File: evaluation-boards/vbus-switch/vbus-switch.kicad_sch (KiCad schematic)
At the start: 83 parts, among them J1 BANANA, J10 01x02, J11 Conn_02x06_Top_Bottom, J2 BANANA, J3 BANANA, J4 USB_C, J5 USB_C, J6 USB_A, J7 01x02, J8 01x02, J9 01x02, Q1 PMOS, Q2 PMOS, Q3 PMOS, Q4 PMOS, Q5 2PMOS, Q6 2NMOS, Q7 2NMOS, U1 PAC195X-1-WLCSP, U2 FUSB302BMPX

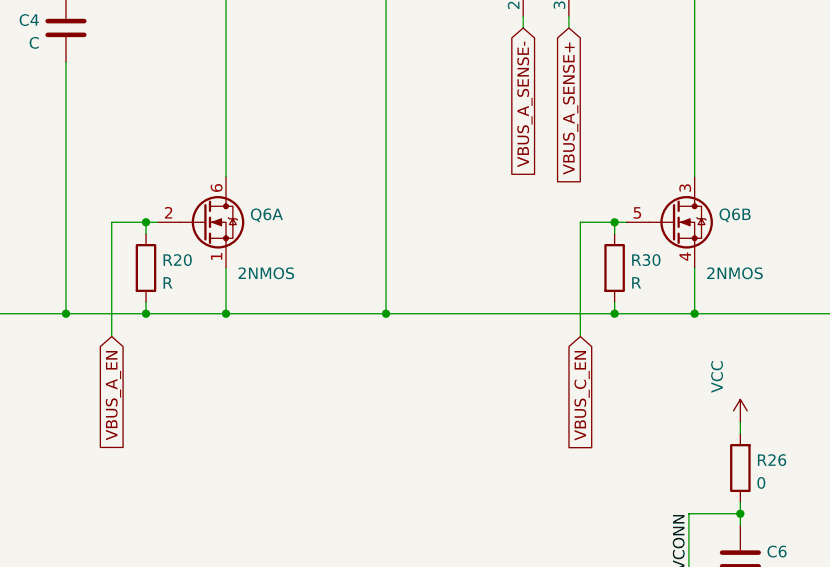
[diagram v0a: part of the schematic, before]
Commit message: vbus-switch: add part selections
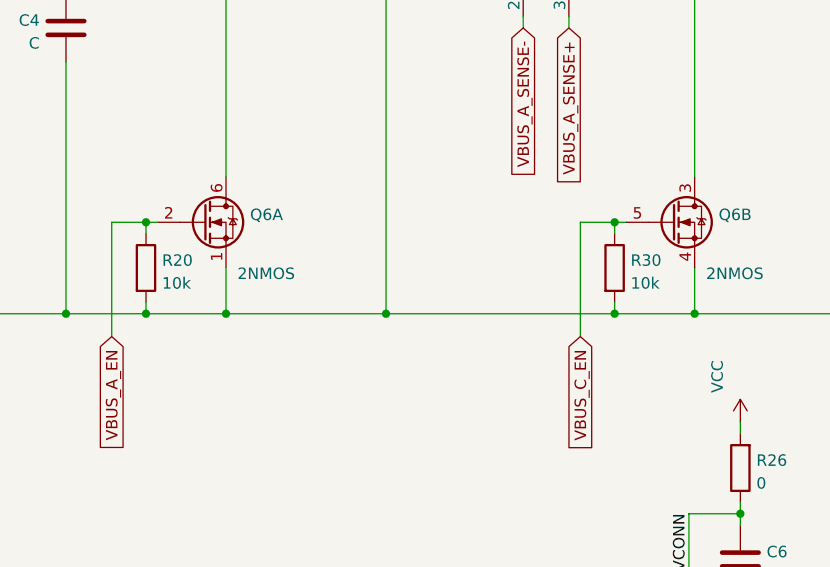
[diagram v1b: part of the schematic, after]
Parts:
- J4, J5: Manufacturer (none) -> XKB; Part Number (none) -> U262-161N-4BVC11
- J6: Manufacturer (none) -> Jing Extension of the Electronic Co.; Part Number (none) -> C42411
- Q1, Q2, Q3, Q4: Manufacturer (none) -> Panjit; Part Number (none) -> PJA3441_R1_00001
- Q5: Manufacturer (none) -> Yangzhou Yangjie; Part Number (none) -> BSS84DW
- Q6, Q7: Manufacturer (none) -> Yangzhou Yangjie; Part Number (none) -> 2N7002DW
- R20, R30: value R -> 10k
- U1: Manufacturer (none) -> Microchip; Part Number (none) -> PAC1954T-E/J6CX
- U2: Manufacturer (none) -> onsemi; Part Number (none) -> FUSB302BMPX
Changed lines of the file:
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@@
+      (effects (font (size 1.27 1.27)) hide)
+    )
+    (property "Manufacturer" "Yangzhou Yangjie" (id 4) (at 191.77 35.56 0)
+      (effects (font (size 1.27 1.27)) hide)
+    )
+    (property "Part Number" "BSS84DW" (id 5) (at 191.77 35.56 0)
       (effects (font (size 1.27 1.27)) hide)
     )
@@
     )
     (property "Datasheet" "~" (id 3) (at 140.97 35.56 0)
+      (effects (font (size 1.27 1.27)) hide)
+    )
+    (property "Manufacturer" "Yangzhou Yangjie" (id 4) (at 139.7 35.56 0)
+      (effects (font (size 1.27 1.27)) hide)
+    )
+    (property "Part Number" "BSS84DW" (id 5) (at 139.7 35.56 0)
       (effects (font (size 1.27 1.27)) hide)
     )
@@
       (effects (font (size 1.27 1.27)) (justify left))
     )
-    (property "Value" "R" (id 1) (at 124.968 85.5222 0)
+    (property "Value" "10k" (id 1) (at 124.968 85.5222 0)
       (effects (font (size 1.27 1.27)) (justify left))
     )
@@
     )
     (property "Datasheet" "" (id 3) (at 103.505 173.355 0)
+      (effects (font (size 1.27 1.27)) hide)
+    )
+    (property "Manufacturer" "Microchip" (id 4) (at 103.505 173.355 0)
+      (effects (font (size 1.27 1.27)) hide)
+    )
+    (property "Part Number" "PAC1954T-E/J6CX" (id 5) (at 103.505 173.355 0)
       (effects (font (size 1.27 1.27)) hide)
     )
@@
       (effects (font (size 1.27 1.27)) hide)
     )
+    (property "Manufacturer" "Panjit" (id 4) (at 93.98 35.56 0)
+      (effects (font (size 1.27 1.27)) hide)
+    )
+    (property "Part Number" "PJA3441_R1_00001" (id 5) (at 93.98 35.56 0)
+      (effects (font (size 1.27 1.27)) hide)
+    )
     (pin "1")
     (pin "2")
@@
     )
     (property "Datasheet" "~" (id 3) (at 72.39 35.56 0)
+      (effects (font (size 1.27 1.27)) hide)
+    )
+    (property "Manufacturer" "Panjit" (id 4) (at 72.39 35.56 0)
+      (effects (font (size 1.27 1.27)) hide)
+    )
+    (property "Part Number" "PJA3441_R1_00001" (id 5) (at 72.39 35.56 0)
       (effects (font (size 1.27 1.27)) hide)
     )
@@
     )
     (property "Datasheet" "https://www.usb.org/sites/default/files/documents/usb_type-c.zip" (id 3) (at 262.255 125.73 0)
+      (effects (font (size 1.27 1.27)) hide)
+    )
+    (property "Manufacturer" "XKB" (id 4) (at 266.065 125.73 0)
+      (effects (font (size 1.27 1.27)) hide)
+    )
+    (property "Part Number" "U262-161N-4BVC11" (id 5) (at 266.065 125.73 0)
       (effects (font (size 1.27 1.27)) hide)
     )
@@
       (effects (font (size 1.27 1.27)) hide)
     )
+    (property "Manufacturer" "Yangzhou Yangjie" (id 4) (at 129.54 78.74 0)
+      (effects (font (size 1.27 1.27)) hide)
+    )
+    (property "Part Number" "2N7002DW" (id 5) (at 129.54 78.74 0)
+      (effects (font (size 1.27 1.27)) hide)
+    )
     (pin "1")
     (pin "2")
@@
       (effects (font (size 1.27 1.27)) hide)
     )
+    (property "Manufacturer" "Panjit" (id 4) (at 210.82 41.91 0)
+      (effects (font (size 1.27 1.27)) hide)
+    )
+    (property "Part Number" "PJA3441_R1_00001" (id 5) (at 210.82 41.91 0)
+      (effects (font (size 1.27 1.27)) hide)
+    )
     (pin "1")
     (pin "2")
@@
       (effects (font (size 1.27 1.27)) (justify left))
     )
-    (property "Value" "R" (id 1) (at 177.038 85.5222 0)
+    (property "Value" "10k" (id 1) (at 177.038 85.5222 0)
       (effects (font (size 1.27 1.27)) (justify left))
     )
@@
       (effects (font (size 1.27 1.27)) hide)
     )
+    (property "Manufacturer" "Jing Extension of the Electronic Co." (id 4) (at 274.955 43.815 0)
+      (effects (font (size 1.27 1.27)) hide)
+    )
+    (property "Part Number" "C42411" (id 5) (at 274.955 43.815 0)
+      (effects (font (size 1.27 1.27)) hide)
+    )
     (pin "1")
     (pin "2")
@@
     )
     (property "Datasheet" "~" (id 3) (at 186.69 78.74 0)
+      (effects (font (size 1.27 1.27)) hide)
+    )
+    (property "Manufacturer" "Yangzhou Yangjie" (id 4) (at 181.61 78.74 0)
+      (effects (font (size 1.27 1.27)) hide)
+    )
+    (property "Part Number" "2N7002DW" (id 5) (at 181.61 78.74 0)
       (effects (font (size 1.27 1.27)) hide)
     )
@@
       (effects (font (size 1.27 1.27)) hide)
     )
+    (property "Manufacturer" "Yangzhou Yangjie" (id 4) (at 82.55 72.39 0)
+      (effects (font (size 1.27 1.27)) hide)
+    )
+    (property "Part Number" "2N7002DW" (id 5) (at 82.55 72.39 0)
+      (effects (font (size 1.27 1.27)) hide)
+    )
     (pin "1")
     (pin "2")
@@
       (effects (font (size 1.27 1.27)) hide)
     )
+    (property "Manufacturer" "Panjit" (id 4) (at 158.75 41.91 0)
+      (effects (font (size 1.27 1.27)) hide)
+    )
+    (property "Part Number" "PJA3441_R1_00001" (id 5) (at 158.75 41.91 0)
+      (effects (font (size 1.27 1.27)) hide)
+    )
     (pin "1")
     (pin "2")
@@
     )
     (property "Datasheet" "http://www.onsemi.com/pub/Collateral/FUSB302B-D.PDF" (id 3) (at 186.055 146.05 0)
+      (effects (font (size 1.27 1.27)) hide)
+    )
+    (property "Manufacturer" "onsemi" (id 4) (at 183.515 135.89 0)
+      (effects (font (size 1.27 1.27)) hide)
+    )
+    (property "Part Number" "FUSB302BMPX" (id 5) (at 183.515 135.89 0)
       (effects (font (size 1.27 1.27)) hide)
     )
@@
     )
     (property "Datasheet" "https://www.usb.org/sites/default/files/documents/usb_type-c.zip" (id 3) (at 33.02 147.32 0)
+      (effects (font (size 1.27 1.27)) hide)
+    )
+    (property "Manufacturer" "XKB" (id 4) (at 29.21 147.32 0)
+      (effects (font (size 1.27 1.27)) hide)
+    )
+    (property "Part Number" "U262-161N-4BVC11" (id 5) (at 29.21 147.32 0)
       (effects (font (size 1.27 1.27)) hide)
     )
@@
       (effects (font (size 1.27 1.27)) hide)
     )
+    (property "Manufacturer" "Yangzhou Yangjie" (id 4) (at 53.975 78.74 0)
+      (effects (font (size 1.27 1.27)) hide)
+    )
+    (property "Part Number" "2N7002DW" (id 5) (at 53.975 78.74 0)
+      (effects (font (size 1.27 1.27)) hide)
+    )
     (pin "1")
     (pin "2")
@@
     )
     (path "/628c65a9-0f43-4685-aa66-ee3ad9642224"
-      (reference "R20") (unit 1) (value "R") (footprint "Resistor_SMD:R_0402_1005Metric")
+      (reference "R20") (unit 1) (value "10k") (footprint "Resistor_SMD:R_0402_1005Metric")
     )
     (path "/1abddf7a-ee92-4556-a8f2-a69dd1f55f62"
@@
     )
     (path "/a4d8816a-0ec1-467c-8ec7-bd93ed44bef5"
-      (reference "R30") (unit 1) (value "R") (footprint "Resistor_SMD:R_0402_1005Metric")
+      (reference "R30") (unit 1) (value "10k") (footprint "Resistor_SMD:R_0402_1005Metric")
     )
     (path "/f2aac2dc-6a47-45ec-8c8f-6020a76a7c4e"

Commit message: update vbus-switch
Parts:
- removed Q5: 2PMOS, Package_TO_SOT_SMD:SOT-363_SC-70-6, symbol Device:Q_Dual_PMOS_S1G1D2S2G2D1
- removed Q6, Q7: 2NMOS, Package_TO_SOT_SMD:SOT-363_SC-70-6, symbol Device:Q_Dual_NMOS_S1G1D2S2G2D1
- removed R31: 20k, Resistor_SMD:R_0402_1005Metric, symbol Device:R
- removed R32, R33: 10k, Resistor_SMD:R_0402_1005Metric, symbol Device:R
- removed R35: 0.02±1%, eval:R_0603_1608Metric_Current_Sense, symbol Device:R_Shunt
- added C11: 2.2uF, Capacitor_SMD:C_0603_1608Metric, symbol Device:C
- added C12: 1uF, Capacitor_SMD:C_0603_1608Metric, symbol Device:C
- added C13, C14, C15, C16: 390pF, Capacitor_SMD:C_0402_1005Metric, symbol Device:C
- added D3, D5: D, Diode_SMD:D_SOD-123F, symbol Device:D_Schottky
- added D4: 6.2±2%, eval:DFN1006-2, symbol Device:D_Zener
- added D6: 18±2%, eval:DFN1006-2, symbol Device:D_Zener
- added D7: 4.7±2%, eval:DFN1006-2, symbol Device:D_Zener
- added J12, J14, J15, J16: 01x02, Connector_PinHeader_2.54mm:PinHeader_1x02_P2.54mm_Vertical, symbol Connector_Generic:Conn_01x02
- added J13: BANANA, Connector:Banana_Jack_2Pin, symbol Connector_Generic:Conn_01x02
- added J17: USB_C, eval:USB_C_Receptacle_HRO_TYPE-C-31-M-12, symbol Connector:USB_C_Receptacle_USB2.0
- added Q1, Q10, Q7: 2NPN, Package_TO_SOT_SMD:SOT-363_SC-70-6, symbol Transistor_BJT:BC847BS
- added Q11, Q12, Q3, Q4: PMOS, Package_TO_SOT_SMD:SOT-23-3, symbol Device:Q_PMOS_GSD
- added Q2: 2PNP, Package_TO_SOT_SMD:SOT-363_SC-70-6, symbol Device:Q_Dual_PNP_PNP_E1B1C2E2B2C1
- added R1, R3, R4, R41, R51: 18.7k±1%, Resistor_SMD:R_0402_1005Metric, symbol Device:R
- added R14, R35, R37, R38, R43, R44, R45: 33k, Resistor_SMD:R_0402_1005Metric, symbol Device:R
- added R40, R42: 2.2k, Resistor_SMD:R_0402_1005Metric, symbol Device:R
- added R46: 0.02±1%, eval:R_0603_1608Metric_Current_Sense, symbol Device:R_Shunt
- added R47: 0, Resistor_SMD:R_0402_1005Metric, symbol Device:R
- added R48: 58.3k±1%, Resistor_SMD:R_0402_1005Metric, symbol Device:R
- added R49, R50, R54: R, Resistor_SMD:R_0402_1005Metric, symbol Device:R
- added R52, R53: 5.1k, Resistor_SMD:R_0402_1005Metric, symbol Device:R
- added TP16: TestPoint, TestPoint:TestPoint_Pad_D1.5mm, symbol Connector:TestPoint
- added U3: AP7361EA-33, Package_DFN_QFN:DFN-8-1EP_3x3mm_P0.65mm_EP1.55x2.4mm, symbol eval:AP7361EA-XXFGE-7
- C1: footprint Capacitor_SMD:C_0805_2012Metric -> Capacitor_SMD:C_0402_1005Metric
- D1: value 5.6±2% -> 4.7±2%; Part Number BZX884-B5V6,315 -> BZX884-B4V7,315
- D2: value 4.7±2% -> 18±2%; DNP (none) -> DNP; Part Number BZX884-B4V7,315 -> BZX884-B18,315
- R13: value 0 -> 2.2k
- R15: value 1k -> 18.7k±1%
- R16: value 20k -> R
- R17, R22, R29, R30: value 10k -> 18.7k±1%
- R18: value 10k -> 33k
- R2, R21: value 20k -> 18.7k±1%
- R20: value 10k -> 2.2k
- R33: renamed from R1; value 20k -> 33k
- R39: renamed from R14; value 1k -> 2.2k
- renumbered Q1 to Q5, Q4 to Q6, Q2 to Q8, Q3 to Q9, R3 to R31, R4 to R32
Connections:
- net VBUS_C_SENSE+ is gone; now on net AUX_SENSE+: U1.A3 (SENSE1+)
- net VBUS_C_SENSE- is gone; now on net AUX_SENSE-: U1.A2 (SENSE1-)
- net +5V: now also C1.1, R16.1, C12.2, D3.1 (K), D4.1 (K), D5.1 (K), J14.1 (Pin_1), J14.2 (Pin_2), U3.5 (EN), U3.8 (IN); no longer C7.1, J1.2 (Pin_2), J4.A4 (VBUS), J4.A9 (VBUS), J4.B4 (VBUS), J4.B9 (VBUS), J7.1 (Pin_1), J7.2 (Pin_2), R32.4
- net GND: now also R16.2, R2.2, R21.2, C11.2, C12.1, C13.1, C14.2, C15.1, C16.2, D4.2 (A), J13.1 (Pin_1), J17.A1 (GND), J17.A12 (GND), J17.B1 (GND), J17.B12 (GND), Q1.1 (E1), Q1.4 (E2), Q10.1 (E1), Q10.4 (E2), Q7.1 (E1), Q7.4 (E2), R37.2, R38.2, R4.2, R43.2, R47.2, R49.2, R50.2, R51.2, R52.2, R53.2, R54.2, U3.4 (GND), U3.9 (GND); no longer D1.2 (A), R20.2, R29.2
- net VCC: now also J16.1 (Pin_1), J16.2 (Pin_2)
- net TARGET_A_VBUS: now reaches Q8.3 (D), R34.1
- net TARGET_A_VBUS: now also Q9.3 (D), TP12.1, Q11.3 (D)
- net AUX_VBUS: now reaches R32.1
- net AUX_VBUS: now also Q6.3 (D), R18.1, R29.1, D6.1 (K), Q2.4 (E2), Q4.3 (D); no longer Q9.3 (D)
- net at R22.1, TP4.1: now also R29.2, D7.1 (K), Q2.5 (B2); no longer R21.1
- net at TP11.1: now also Q6.1 (G), Q9.1 (G), Q7.3 (C2), R35.2
- net at Q8.1 (G), R33.2, TP10.1: now also Q5.1 (G), Q7.6 (C1); no longer R29.1
- net at J4.B5 (CC2), R6.1: now also C15.2
- net at R22.2: now also Q1.3 (C2)
- net CONTROL_VBUS: now reaches R31.4
- net CONTROL_VBUS: now also D2.1 (K), Q5.3 (D), Q2.1 (E1), Q3.3 (D), R1.1, R14.1; no longer Q6.3 (D)
- net at D2.2 (A), R15.1: now also TP2.1, Q2.6 (C1), Q3.1 (G), R14.2; no longer TP13.1
- net at J4.A5 (CC1), R7.1: now also C16.1
- net at R18.2: now also R17.1, TP3.1, D6.2 (A), Q2.3 (C2), Q4.1 (G)
- net 5V_OUT_EN renamed CONTROL_VBUS_EN
- net 5V_SENSE+ renamed AUX_SENSE+
- net AUX_SENSE+: no longer U1.D3 (SENSE4+)
- net 5V_SENSE- renamed AUX_SENSE-
- net AUX_SENSE-: no longer U1.D2 (SENSE4-)
- net CAP_SENSE+ renamed CONTROL_SENSE+
- net CONTROL_SENSE+: now also U1.A1 (SENSE2+); no longer U1.D1 (SENSE3+)
- net CAP_SENSE- renamed CONTROL_SENSE-
- net CONTROL_SENSE-: now also U1.B1 (SENSE2-); no longer U1.C1 (SENSE3-)
- removed net VBUS: C4.1, D2.1 (K), Q5.2 (S), Q6.2 (S), Q8.2 (S), Q9.2 (S), R16.1, R2.1, R21.2, R33.1, TP15.1
- net VBUS_A renamed TARGET_A_VBUS_CONN
- net VBUS_A_EN: no longer names the net of R20.1
- net VBUS_A_EN: now also R21.1, Q1.5 (B2); no longer J11.8 (Pin_8)
- net VBUS_A_SENSE+ renamed TARGET_A_SENSE+
- net TARGET_A_SENSE+: now also U1.D3 (SENSE4+); no longer U1.A1 (SENSE2+)
- net VBUS_A_SENSE- renamed TARGET_A_SENSE-
- net TARGET_A_SENSE-: now also U1.D2 (SENSE4-); no longer U1.B1 (SENSE2-)
- net VBUS_C renamed TARGET_C_VBUS_CONN
- net TARGET_C_VBUS_CONN: now also R46.4, R50.1; no longer U2.2 (VBUS)
- removed net VBUS_CAP: C1.1, R13.1, R31.1, TP1.1
- net VBUS_C_EN: no longer names the net of R30.1
- net VBUS_C_EN: now also D7.2 (A); no longer J11.7 (Pin_7)
- new net: Q10.2 (B1), R42.1, R43.1
- new net: Q1.2 (B1), R13.1, R4.1
- new net: D1.1 (K), Q2.2 (B1), R1.2, R3.1, TP1.1
- new net: D5.2 (A), Q4.2 (S)
- new net: C11.1, J15.1 (Pin_1), J15.2 (Pin_2), R48.1, U3.1 (OUT)
- new net: R48.2, R51.1, U3.3 (ADJ/NC)
- new net: Q7.5 (B2), R38.1, R40.1
- new net: D1.2 (A), R2.1
- new net: Q1.6 (C1), R3.2
- new net: Q5.2 (S), Q8.2 (S), R33.1
- new net: Q7.2 (B1), R37.1, R39.1
- new net: Q10.3 (C2), Q11.1 (G), Q12.1 (G), R45.2, TP14.1
- new net: Q10.5 (B2), Q10.6 (C1), R44.2, TP13.1
- new net: Q6.2 (S), Q9.2 (S), R35.1
- new net: C14.1, J17.A5 (CC1), R53.1
- new net: Q11.2 (S), Q12.2 (S), R44.1, R45.1
- new net: C13.2, J17.B5 (CC2), R52.1
- new net: J17.S1 (SHIELD), R47.1
- new net: D3.2 (A), Q3.2 (S)
- new net: R41.2, U2.2 (VBUS)
- new net AUX_VBUS_CONN: C4.1, J12.1 (Pin_1), J12.2 (Pin_2), J13.2 (Pin_2), J17.A4 (VBUS), J17.A9 (VBUS), J17.B4 (VBUS), J17.B9 (VBUS), R32.4, R54.1
- new net AUX_VBUS_EN: J11.8 (Pin_8), R40.2
- new net CONTROL_VBUS_CONN: C7.1, J1.2 (Pin_2), J4.A4 (VBUS), J4.A9 (VBUS), J4.B4 (VBUS), J4.B9 (VBUS), J7.1 (Pin_1), J7.2 (Pin_2), R31.1, R49.1
- new net TARGET_C_SENSE+: R46.3, U1.D1 (SENSE3+)
- new net TARGET_C_SENSE-: R46.2, U1.C1 (SENSE3-)
- new net TARGET_C_VBUS: Q12.3 (D), R41.1, R46.1
- new net ~{AUX_VBUS_IN_EN}: R20.2, TP16.1
- new net ~{CONTROL_VBUS_IN_EN}: R13.2, TP15.1
- new net ~{TARGET_C_VBUS_EN}: J11.7 (Pin_7), R42.2
- no-connect marks 14 -> 20
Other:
- note removed: "protect +5V by switching off Q3 and Q4 if VBUS exceeds 5.5 V (absolute max 6.5 V)"
- moved on the sheet: C10, C2, C3, C5, C6, C7, C8, C9, J1, J10, J11, J2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
